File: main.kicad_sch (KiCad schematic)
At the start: 0 parts

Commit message: First finished draft
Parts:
- added H1, H2, H3, H4, H5, H6, H7, H8: MountingHole_Pad, SamacSys_Parts:MountingHole_3.7mm_Pad_Via_Norelief, symbol Mechanical:MountingHole_Pad
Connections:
- net GND: now also H1.1, H2.1, H3.1, H4.1, H5.1, H6.1, H7.1, H8.1
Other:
- added sheet Digital_Utility (digi_util.kicad_sch)

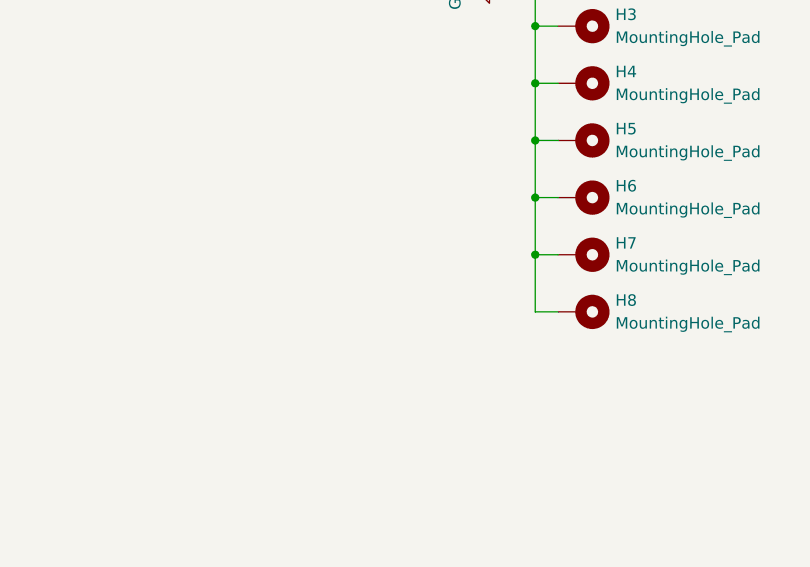
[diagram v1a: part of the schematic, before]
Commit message: Moved 3.3VA supply out of the ADC area, to have that area cleaner
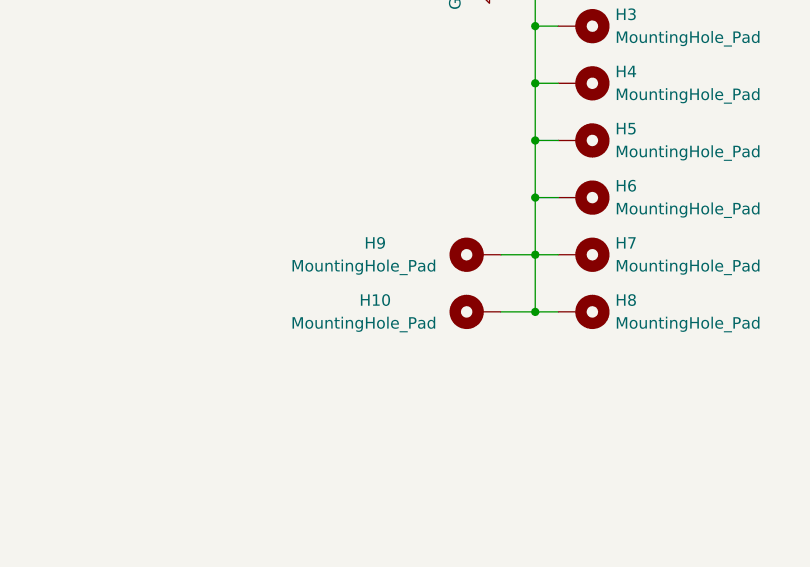
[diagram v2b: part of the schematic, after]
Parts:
- added H10, H9: MountingHole_Pad, SamacSys_Parts:MountingHole_3mm_Pad_Via_Norelief, symbol Mechanical:MountingHole_Pad
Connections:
- net GND: now also H10.1, H9.1
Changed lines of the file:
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@@
   (junction (at 247.65 86.36) (diameter 0) (color 0 0 0 0)
+  )
+  (junction (at 247.65 111.76) (diameter 0) (color 0 0 0 0)
   )
   (junction (at 247.65 105.41) (diameter 0) (color 0 0 0 0)
@@
     (stroke (width 0) (type default) (color 0 0 0 0))
   )
+  (wire (pts (xy 243.84 111.76) (xy 247.65 111.76))
+    (stroke (width 0) (type default) (color 0 0 0 0))
+  )
   (wire (pts (xy 247.65 99.06) (xy 247.65 105.41))
     (stroke (width 0) (type default) (color 0 0 0 0))
@@
     (stroke (width 0) (type default) (color 0 0 0 0))
   )
+  (wire (pts (xy 243.84 105.41) (xy 247.65 105.41))
+    (stroke (width 0) (type default) (color 0 0 0 0))
+  )
   (wire (pts (xy 247.65 80.01) (xy 250.19 80.01))
     (stroke (width 0) (type default) (color 0 0 0 0))
@@
     (at 25.4 173.99 0)
     (effects (font (size 1.27 1.27)) (justify left bottom))
+  )
+  (symbol (lib_id "Mechanical:MountingHole_Pad") (at 241.3 105.41 90) (unit 1)
+    (in_bom yes) (on_board yes)
+    (property "Reference" "H9" (id 0) (at 229.87 104.14 90))
+    (property "Value" "MountingHole_Pad" (id 1) (at 228.6 106.68 90))
+    (property "Footprint" "SamacSys_Parts:MountingHole_3mm_Pad_Via_Norelief" (id 2) (at 241.3 105.41 0)
+      (effects (font (size 1.27 1.27)) hide)
+    )
+    (property "Datasheet" "~" (id 3) (at 241.3 105.41 0)
+      (effects (font (size 1.27 1.27)) hide)
+    )
+    (pin "1")
   )
   (symbol (lib_id "Mechanical:MountingHole_Pad") (at 252.73 105.41 270) (unit 1)
@@
       (effects (font (size 1.27 1.27)) hide)
     )
+    (pin "1")
+  )
+  (symbol (lib_id "Mechanical:MountingHole_Pad") (at 241.3 111.76 90) (unit 1)
+    (in_bom yes) (on_board yes)
+    (property "Reference" "H10" (id 0) (at 229.87 110.49 90))
+    (property "Value" "MountingHole_Pad" (id 1) (at 228.6 113.03 90))
+    (property "Footprint" "SamacSys_Parts:MountingHole_3mm_Pad_Via_Norelief" (id 2) (at 241.3 111.76 0)
+      (effects (font (size 1.27 1.27)) hide)
+    )
+    (property "Datasheet" "~" (id 3) (at 241.3 111.76 0)
+      (effects (font (size 1.27 1.27)) hide)
+    )

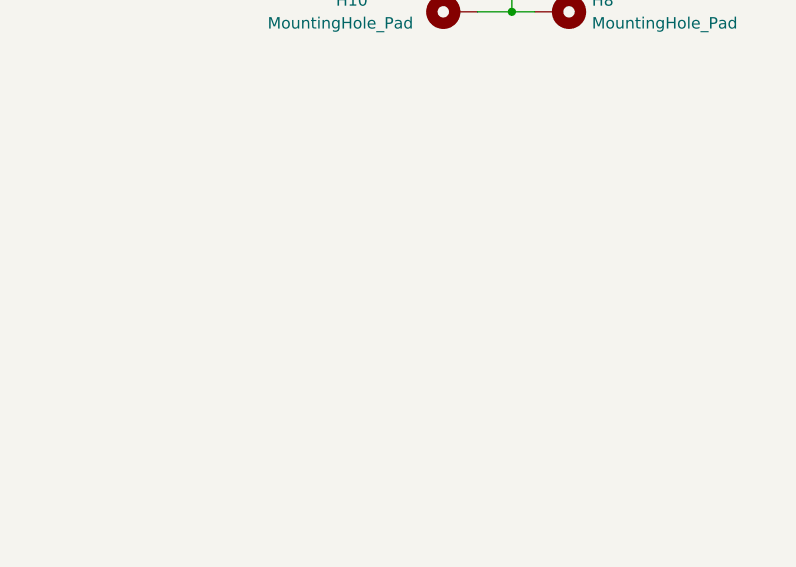
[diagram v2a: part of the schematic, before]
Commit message: First finished version. Still need to check some footprint for critical parts and also refine the part numbers before order
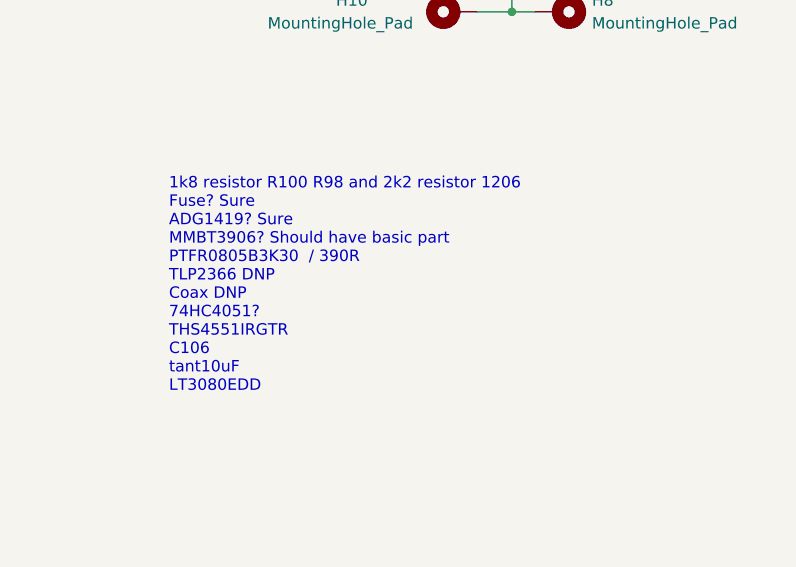
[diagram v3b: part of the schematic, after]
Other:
- note added: "1k8 resistor R100 R98 and 2k2 resistor 1206 Fuse? Sure ADG1419? Sure MMBT3906? Should have basic part PTFR0805B3K30 / 390R TLP2366 DNP Coax DNP 74HC4051? THS4551IRGTR C106 tant10uF LT3080EDD"
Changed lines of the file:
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@@
+    (effects (font (size 1.27 1.27)) (justify left bottom))
+  )
+  (text "1k8 resistor R100 R98 and 2k2 resistor 1206\nFuse? Sure\nADG1419? Sure\nMMBT3906? Should have basic part\nPTFR0805B3K30  / 390R\nTLP2366 DNP\nCoax DNP\n74HC4051?\nTHS4551IRGTR\nC106\ntant10uF\nLT3080EDD\n\n"
+    (at 209.55 156.21 0)
     (effects (font (size 1.27 1.27)) (justify left bottom))
   )

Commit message: Version 1.0 submitted to JLCPCB
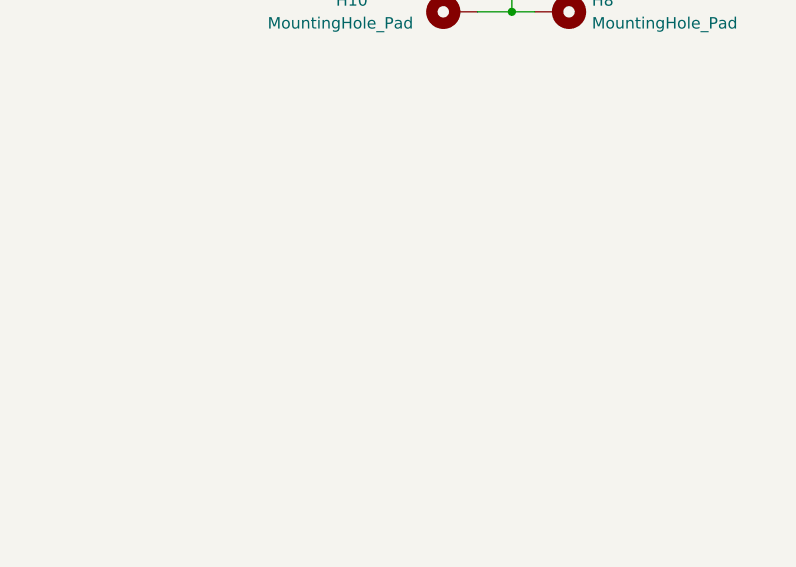
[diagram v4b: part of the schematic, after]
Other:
- note removed: "1k8 resistor R100 R98 and 2k2 resistor 1206 Fuse? Sure ADG1419? Sure MMBT3906? Should have basic part PTFR0805B3K30 / 390R TLP2366 DNP Coax DNP 74HC4051? THS4551IRGTR C106 tant10uF LT3080EDD"
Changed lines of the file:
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@@
-    (effects (font (size 1.27 1.27)) (justify left bottom))
-  )
-  (text "1k8 resistor R100 R98 and 2k2 resistor 1206\nFuse? Sure\nADG1419? Sure\nMMBT3906? Should have basic part\nPTFR0805B3K30  / 390R\nTLP2366 DNP\nCoax DNP\n74HC4051?\nTHS4551IRGTR\nC106\ntant10uF\nLT3080EDD\n\n"
-    (at 209.55 156.21 0)
     (effects (font (size 1.27 1.27)) (justify left bottom))
   )
